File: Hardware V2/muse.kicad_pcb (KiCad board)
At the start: 2 copper layers, 71.6 x 61.5 mm, 53 parts, among them P1 3.5mm_line, P2 3.5mm_line, P3 RCA, P4 RCA, P8 ATX_PS_ON, P9 LED_Signal, Q1 FQP30N06L, Q2 FQP30N06L, Q3 FQP30N06L, Q4 FQP30N06L, Q5 FQP30N06L, Q6 FQP30N06L, SW1 PWR_SW, U1 MSGEQ7, U2 MSGEQ7, U3 74LS595, U4 Spark_Core

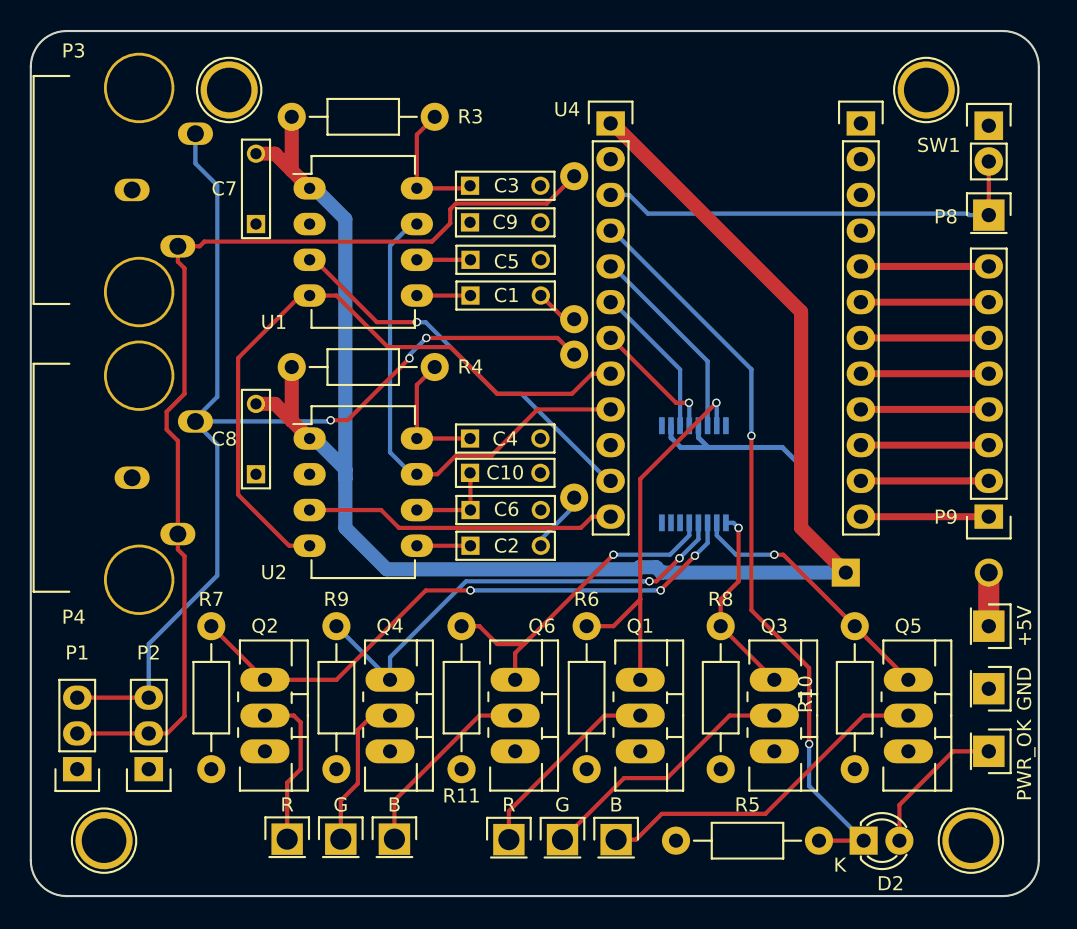
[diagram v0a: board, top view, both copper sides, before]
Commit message: Added more ground paths to v2
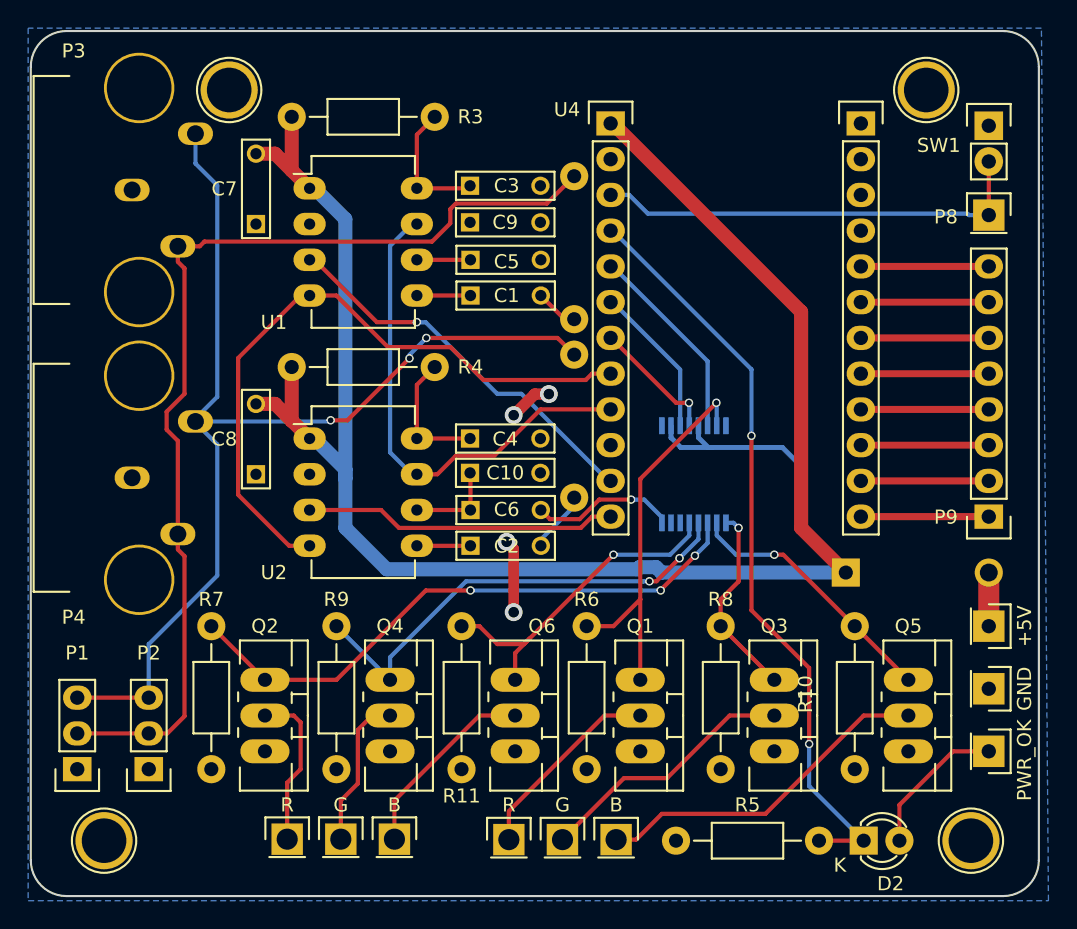
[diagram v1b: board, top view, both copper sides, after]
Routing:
- net GND: track 0.00 -> 10.4 mm, vias 0 -> 1
- net (no net): track 0.00 -> 8.33 mm, vias 0 -> 4
- net /STROBE: track 48.1 -> 47.3 mm
- added copper zone on B.Cu, net GND
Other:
- board text added: "(2.0)"
- board text removed: "(1.0)"
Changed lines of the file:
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@@
 (kicad_pcb (version 4) (host pcbnew 4.0.0-stable)
   (general
-    (links 109)
-    (no_connects 50)
-    (area 83.617999 70.663999 155.396001 132.282001)
+    (links 100)
+    (no_connects 3)
+    (area 82.434286 70.663999 156.111429 133.055)
     (thickness 1.6)
     (drawings 11)
-    (tracks 258)
+    (tracks 275)
     (zones 0)
     (modules 53)
@@
     )
   )
-  (gr_text "(1.0)" (at 145.923 94.234 90) (layer B.SilkS)
+  (gr_text "(2.0)" (at 145.923 94.234 90) (layer B.SilkS)
     (effects (font (size 1 1) (thickness 0.2)) (justify left mirror))
   )
@@
   (gr_line (start 155.321 73.279) (end 155.321 129.667) (layer Edge.Cuts) (width 0.15))
   (gr_line (start 86.233 70.739) (end 152.781 70.739) (layer Edge.Cuts) (width 0.15))
+  (segment (start 118.005 112.035) (end 118.005 107.535) (width 0.762) (layer F.Cu) (net 0))
+  (via (at 117.505 107.035) (size 1.27) (drill 0.762) (layers F.Cu B.Cu) (net 0))
+  (segment (start 118.005 107.535) (end 117.505 107.035) (width 0.762) (layer F.Cu) (net 0))
+  (via (at 118.005 112.035) (size 1.27) (drill 0.762) (layers F.Cu B.Cu) (net 0))
+  (segment (start 118.005 98.035) (end 119.505 96.535) (width 0.808) (layer F.Cu) (net 0))
+  (segment (start 119.505 96.535) (end 120.505 96.535) (width 0.808) (layer F.Cu) (net 0))
+  (via (at 120.505 96.535) (size 1.27) (drill 0.762) (layers F.Cu B.Cu) (net 0))
+  (via (at 118.005 98.035) (size 1.27) (drill 0.762) (layers F.Cu B.Cu) (net 0))
   (segment (start 114.935 89.535) (end 111.125 89.535) (width 0.3) (layer F.Cu) (net 1) (status 30))
   (segment (start 119.935 89.535) (end 121.615 91.215) (width 0.3) (layer F.Cu) (net 2))
@@
   (segment (start 111.125 78.105) (end 112.395 76.835) (width 0.3) (layer F.Cu) (net 5) (status 20))
   (segment (start 111.125 81.915) (end 111.125 78.105) (width 0.3) (layer F.Cu) (net 5) (status 10))
+  (segment (start 126.34999 104.035) (end 127.285 104.035) (width 0.3) (layer B.Cu) (net 6))
+  (segment (start 127.285 104.035) (end 128.535 105.285) (width 0.3) (layer B.Cu) (net 6))
+  (segment (start 128.535 105.285) (end 128.535 105.685) (width 0.3) (layer B.Cu) (net 6))
+  (segment (start 119.935 104.775) (end 120.584999 105.424999) (width 0.3) (layer F.Cu) (net 6))
+  (segment (start 120.584999 105.424999) (end 122.691971 105.424999) (width 0.3) (layer F.Cu) (net 6))
+  (segment (start 122.691971 105.424999) (end 124.084852 104.032118) (width 0.3) (layer F.Cu) (net 6))
+  (segment (start 124.084852 104.032118) (end 126.347108 104.032118) (width 0.3) (layer F.Cu) (net 6))
+  (segment (start 126.347108 104.032118) (end 126.34999 104.035) (width 0.3) (layer F.Cu) (net 6))
+  (via (at 126.34999 104.035) (size 0.6) (drill 0.4) (layers F.Cu B.Cu) (net 6))
   (segment (start 111.125 99.695) (end 115.015 99.695) (width 0.3) (layer F.Cu) (net 7) (status 30))
   (segment (start 111.125 95.885) (end 112.395 94.615) (width 0.3) (layer F.Cu) (net 7) (status 20))
@@
   (segment (start 105.41 89.535) (end 109.075 93.2) (width 0.3) (layer F.Cu) (net 36))
   (segment (start 109.075 93.2) (end 113.52 93.2) (width 0.3) (layer F.Cu) (net 36))
-  (segment (start 113.52 93.2) (end 116.84 96.52) (width 0.3) (layer F.Cu) (net 36))
-  (segment (start 116.84 96.52) (end 122.14409 96.52) (width 0.3) (layer F.Cu) (net 36))
-  (segment (start 122.14409 96.52) (end 123.578362 95.085728) (width 0.3) (layer F.Cu) (net 36))
+  (segment (start 113.52 93.2) (end 115.855 95.535) (width 0.3) (layer F.Cu) (net 36))
+  (segment (start 115.855 95.535) (end 123.12909 95.535) (width 0.3) (layer F.Cu) (net 36))
+  (segment (start 123.12909 95.535) (end 123.578362 95.085728) (width 0.3) (layer F.Cu) (net 36))
   (segment (start 123.578362 95.085728) (end 124.894362 95.085728) (width 0.3) (layer F.Cu) (net 36))
   (segment (start 102.87 89.535) (end 103.505 89.535) (width 0.3) (layer F.Cu) (net 36) (status 30))
@@
   (segment (start 103.505 107.315) (end 102.055 107.315) (width 0.3) (layer F.Cu) (net 36) (status 10))
   (segment (start 111.125 102.235) (end 112.575 102.235) (width 0.3) (layer F.Cu) (net 37))
+  (segment (start 119.914272 97.625728) (end 124.894362 97.625728) (width 0.3) (layer F.Cu) (net 37))
   (segment (start 112.575 102.235) (end 113.905 100.905) (width 0.3) (layer F.Cu) (net 37))
-  (segment (start 113.905 100.905) (end 116.425728 100.905) (width 0.3) (layer F.Cu) (net 37))
-  (segment (start 116.425728 100.905) (end 119.705 97.625728) (width 0.3) (layer F.Cu) (net 37))
-  (segment (start 119.705 97.625728) (end 124.894362 97.625728) (width 0.3) (layer F.Cu) (net 37))
+  (segment (start 113.905 100.905) (end 116.635 100.905) (width 0.3) (layer F.Cu) (net 37))
+  (segment (start 116.635 100.905) (end 119.914272 97.625728) (width 0.3) (layer F.Cu) (net 37))
   (segment (start 110.775 84.455) (end 111.125 84.455) (width 0.3) (layer B.Cu) (net 37) (status 30))
   (segment (start 109.22 86.01) (end 110.775 84.455) (width 0.3) (layer B.Cu) (net 37) (status 20))
@@
   (segment (start 150.239518 83.712118) (end 150.3474 83.82) (width 0.3) (layer B.Cu) (net 44))
   (segment (start 150.3474 83.82) (end 151.765 83.82) (width 0.3) (layer B.Cu) (net 44))
+  (zone (net 6) (net_name GND) (layer B.Cu) (hatch edge 0.508)
+    (connect_pads (clearance 0.508))
+    (min_thickness 0.254)
+    (fill yes (arc_segments 16) (thermal_gap 0.508) (thermal_bridge_width 0.508))
+    (polygon
+      (pts
+        (xy 83.505 70.535) (xy 83.505 132.535) (xy 156.005 132.535) (xy 155.505 70.535)
+      )
+    )
+  )
 )

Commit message: Gerbers generated and sent to Oshpark
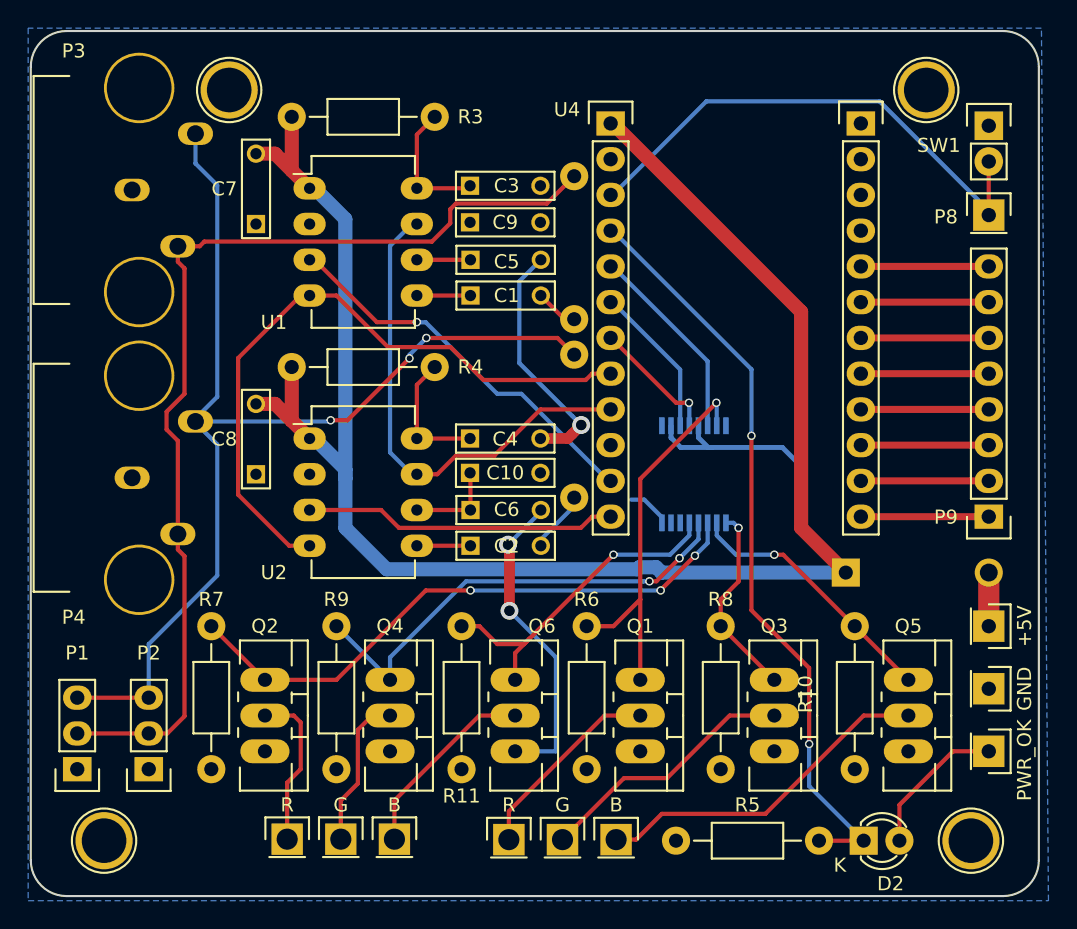
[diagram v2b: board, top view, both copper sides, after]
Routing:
- net GND: track 10.4 -> 43.0 mm, vias 1 -> 3
- net (no net): track 8.33 -> 0.00 mm, vias 4 -> 0
- net /ATX_PWR_ON: track 27.5 -> 33.2 mm
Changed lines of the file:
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@@
     (links 100)
     (no_connects 3)
-    (area 82.434286 70.663999 156.111429 133.055)
+    (area 83.617999 70.663999 155.396001 132.282001)
     (thickness 1.6)
     (drawings 11)
-    (tracks 275)
+    (tracks 278)
     (zones 0)
     (modules 53)
@@
     (visible_elements FFFFFF7F)
     (pcbplotparams
-      (layerselection 0x00030_80000001)
+      (layerselection 0x010f0_80000001)
       (usegerberextensions false)
       (excludeedgelayer true)
@@
       (outputformat 1)
       (mirror false)
-      (drillshape 1)
+      (drillshape 0)
       (scaleselection 1)
-      (outputdirectory ""))
+      (outputdirectory Gerbers/))
   )
   (net 0 "")
@@
   (gr_line (start 155.321 73.279) (end 155.321 129.667) (layer Edge.Cuts) (width 0.15))
   (gr_line (start 86.233 70.739) (end 152.781 70.739) (layer Edge.Cuts) (width 0.15))
-  (segment (start 118.005 112.035) (end 118.005 107.535) (width 0.762) (layer F.Cu) (net 0))
-  (via (at 117.505 107.035) (size 1.27) (drill 0.762) (layers F.Cu B.Cu) (net 0))
-  (segment (start 118.005 107.535) (end 117.505 107.035) (width 0.762) (layer F.Cu) (net 0))
-  (via (at 118.005 112.035) (size 1.27) (drill 0.762) (layers F.Cu B.Cu) (net 0))
-  (segment (start 118.005 98.035) (end 119.505 96.535) (width 0.808) (layer F.Cu) (net 0))
-  (segment (start 119.505 96.535) (end 120.505 96.535) (width 0.808) (layer F.Cu) (net 0))
-  (via (at 120.505 96.535) (size 1.27) (drill 0.762) (layers F.Cu B.Cu) (net 0))
-  (via (at 118.005 98.035) (size 1.27) (drill 0.762) (layers F.Cu B.Cu) (net 0))
   (segment (start 114.935 89.535) (end 111.125 89.535) (width 0.3) (layer F.Cu) (net 1) (status 30))
   (segment (start 119.935 89.535) (end 121.615 91.215) (width 0.3) (layer F.Cu) (net 2))
@@
   (segment (start 111.125 78.105) (end 112.395 76.835) (width 0.3) (layer F.Cu) (net 5) (status 20))
   (segment (start 111.125 81.915) (end 111.125 78.105) (width 0.3) (layer F.Cu) (net 5) (status 10))
+  (segment (start 119.905 99.695) (end 121.845 99.695) (width 0.762) (layer F.Cu) (net 6))
+  (segment (start 122.170001 99.369999) (end 122.805 98.735) (width 0.762) (layer F.Cu) (net 6))
+  (segment (start 122.170001 98.100001) (end 122.805 98.735) (width 0.3) (layer B.Cu) (net 6))
+  (segment (start 121.845 99.695) (end 122.170001 99.369999) (width 0.762) (layer F.Cu) (net 6))
+  (segment (start 118.405 94.335) (end 122.170001 98.100001) (width 0.3) (layer B.Cu) (net 6))
+  (segment (start 118.405 88.525) (end 118.405 94.335) (width 0.3) (layer B.Cu) (net 6))
+  (segment (start 119.935 86.995) (end 118.405 88.525) (width 0.3) (layer B.Cu) (net 6))
+  (via (at 122.805 98.735) (size 1.27) (drill 0.762) (layers F.Cu B.Cu) (net 6))
+  (segment (start 118.11 121.92) (end 121.005 121.92) (width 0.3) (layer B.Cu) (net 6))
+  (segment (start 121.005 121.92) (end 121.005 115.235) (width 0.3) (layer B.Cu) (net 6))
+  (segment (start 121.005 115.235) (end 117.705 111.935) (width 0.3) (layer B.Cu) (net 6))
+  (segment (start 117.605 107.235) (end 119.935 104.905) (width 0.3) (layer B.Cu) (net 6))
+  (segment (start 119.935 104.905) (end 119.935 104.775) (width 0.3) (layer B.Cu) (net 6))
+  (segment (start 117.705 111.935) (end 117.705 107.335) (width 0.762) (layer F.Cu) (net 6))
+  (segment (start 117.705 107.335) (end 117.605 107.235) (width 0.762) (layer F.Cu) (net 6))
+  (via (at 117.605 107.235) (size 1.27) (drill 0.762) (layers F.Cu B.Cu) (net 6))
+  (via (at 117.705 111.935) (size 1.27) (drill 0.762) (layers F.Cu B.Cu) (net 6))
   (segment (start 126.34999 104.035) (end 127.285 104.035) (width 0.3) (layer B.Cu) (net 6))
   (segment (start 127.285 104.035) (end 128.535 105.285) (width 0.3) (layer B.Cu) (net 6))
   (segment (start 128.535 105.285) (end 128.535 105.685) (width 0.3) (layer B.Cu) (net 6))
-  (segment (start 119.935 104.775) (end 120.584999 105.424999) (width 0.3) (layer F.Cu) (net 6))
-  (segment (start 120.584999 105.424999) (end 122.691971 105.424999) (width 0.3) (layer F.Cu) (net 6))
-  (segment (start 122.691971 105.424999) (end 124.084852 104.032118) (width 0.3) (layer F.Cu) (net 6))
-  (segment (start 124.084852 104.032118) (end 126.347108 104.032118) (width 0.3) (layer F.Cu) (net 6))
-  (segment (start 126.347108 104.032118) (end 126.34999 104.035) (width 0.3) (layer F.Cu) (net 6))
-  (via (at 126.34999 104.035) (size 0.6) (drill 0.4) (layers F.Cu B.Cu) (net 6))
   (segment (start 111.125 99.695) (end 115.015 99.695) (width 0.3) (layer F.Cu) (net 7) (status 30))
   (segment (start 111.125 95.885) (end 112.395 94.615) (width 0.3) (layer F.Cu) (net 7) (status 20))
@@
   (segment (start 134.9 94.778966) (end 134.9 99.5) (width 0.3) (layer B.Cu) (net 43))
   (via (at 134.9 99.5) (size 0.6) (drill 0.4) (layers F.Cu B.Cu) (net 43))
-  (segment (start 124.894362 82.385728) (end 126.210362 82.385728) (width 0.3) (layer B.Cu) (net 44))
-  (segment (start 126.210362 82.385728) (end 127.536752 83.712118) (width 0.3) (layer B.Cu) (net 44))
-  (segment (start 127.536752 83.712118) (end 150.239518 83.712118) (width 0.3) (layer B.Cu) (net 44))
-  (segment (start 150.239518 83.712118) (end 150.3474 83.82) (width 0.3) (layer B.Cu) (net 44))
-  (segment (start 150.3474 83.82) (end 151.765 83.82) (width 0.3) (layer B.Cu) (net 44))
+  (segment (start 124.894362 82.385728) (end 125.046762 82.385728) (width 0.3) (layer B.Cu) (net 44))
+  (segment (start 125.046762 82.385728) (end 131.69749 75.735) (width 0.3) (layer B.Cu) (net 44))
+  (segment (start 151.765 83.495) (end 151.765 83.82) (width 0.3) (layer B.Cu) (net 44))
+  (segment (start 131.69749 75.735) (end 144.005 75.735) (width 0.3) (layer B.Cu) (net 44))
+  (segment (start 144.005 75.735) (end 151.765 83.495) (width 0.3) (layer B.Cu) (net 44))
   (zone (net 6) (net_name GND) (layer B.Cu) (hatch edge 0.508)
     (connect_pads (clearance 0.508))
